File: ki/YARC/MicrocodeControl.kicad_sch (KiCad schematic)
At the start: 24 parts, among them U31 74LS32, U44 74LS574, U45 74LS574, U46 74LS157, U47 74LS157, U48 74LS193, U49 74LS193, U50 74LS139, U51 74LS32, U52 74LS32, U53 74LS157, U54 74LS32

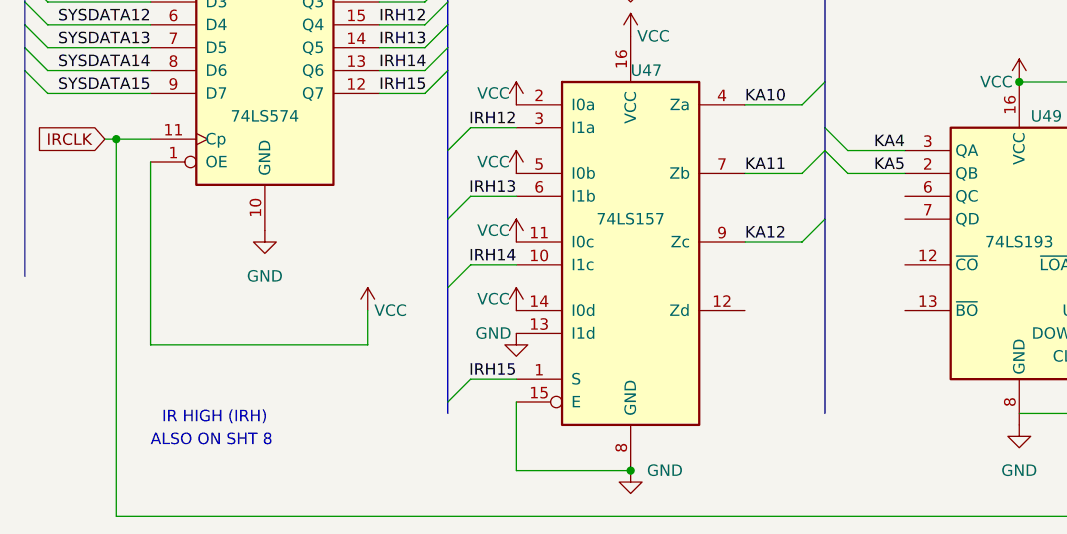
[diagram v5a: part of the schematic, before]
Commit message: Fix - add microcode RAM enables to schematic
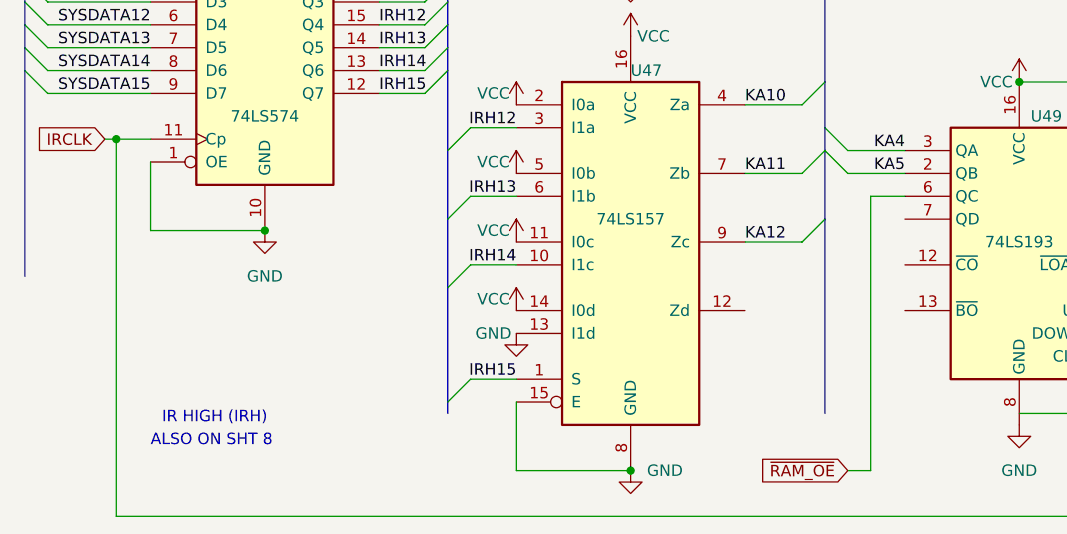
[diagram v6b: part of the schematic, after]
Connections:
- net GND: now also U44.1 (OE)
- net VCC: no longer U44.1 (OE)
- net ~{RAM_OE}: now reaches U49.6 (QC)
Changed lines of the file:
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@@
   (junction (at 209.55 67.31) (diameter 0) (color 0 0 0 0)
   )
+  (junction (at 40.64 170.18) (diameter 0) (color 0 0 0 0)
+  )
   (junction (at 209.55 29.21) (diameter 0) (color 0 0 0 0)
   )
@@
     (stroke (width 0) (type default) (color 0 0 0 0))
   )
-  (wire (pts (xy 52.07 179.07) (xy 52.07 182.88))
-    (stroke (width 0) (type default) (color 0 0 0 0))
-  )
   (bus (pts (xy 13.97 144.78) (xy 13.97 142.24))
     (stroke (width 0) (type default) (color 0 0 0 0))
@@
     (stroke (width 0) (type default) (color 0 0 0 0))
   )
-  (wire (pts (xy 27.94 182.88) (xy 52.07 182.88))
-    (stroke (width 0) (type default) (color 0 0 0 0))
-  )
   (wire (pts (xy 100.33 124.46) (xy 93.98 124.46))
     (stroke (width 0) (type default) (color 0 0 0 0))
@@
     (stroke (width 0) (type default) (color 0 0 0 0))
   )
+  (wire (pts (xy 105.41 196.85) (xy 107.95 196.85))
+    (stroke (width 0) (type default) (color 0 0 0 0))
+  )
   (wire (pts (xy 55.88 38.1) (xy 86.36 38.1))
     (stroke (width 0) (type default) (color 0 0 0 0))
@@
     (stroke (width 0) (type default) (color 0 0 0 0))
   )
+  (wire (pts (xy 27.94 170.18) (xy 40.64 170.18))
+    (stroke (width 0) (type default) (color 0 0 0 0))
+  )
   (wire (pts (xy 142.24 143.51) (xy 142.24 179.07))
     (stroke (width 0) (type default) (color 0 0 0 0))
@@
     (stroke (width 0) (type default) (color 0 0 0 0))
   )
-  (wire (pts (xy 27.94 162.56) (xy 27.94 182.88))
-    (stroke (width 0) (type default) (color 0 0 0 0))
-  )
   (wire (pts (xy 137.16 181.61) (xy 149.86 181.61))
     (stroke (width 0) (type default) (color 0 0 0 0))
@@
     (stroke (width 0) (type default) (color 0 0 0 0))
   )
+  (wire (pts (xy 107.95 166.37) (xy 107.95 196.85))
+    (stroke (width 0) (type default) (color 0 0 0 0))
+  )
   (wire (pts (xy 229.87 39.37) (xy 245.11 39.37))
     (stroke (width 0) (type default) (color 0 0 0 0))
@@
     (stroke (width 0) (type default) (color 0 0 0 0))
   )
+  (wire (pts (xy 111.76 166.37) (xy 107.95 166.37))
+    (stroke (width 0) (type default) (color 0 0 0 0))
+  )
   (wire (pts (xy 160.02 85.09) (xy 190.5 85.09))
     (stroke (width 0) (type default) (color 0 0 0 0))
@@
     (stroke (width 0) (type default) (color 0 0 0 0))
   )
+  (wire (pts (xy 27.94 162.56) (xy 27.94 170.18))
+    (stroke (width 0) (type default) (color 0 0 0 0))
+  )
   (wire (pts (xy 209.55 36.83) (xy 209.55 29.21))
     (stroke (width 0) (type default) (color 0 0 0 0))
@@
   (label "KX3" (at 30.48 38.1 180)
     (effects (font (size 1.27 1.27)) (justify right bottom))
+  )
+  (global_label "~{RAM_OE}" (shape input) (at 105.41 196.85 180) (fields_autoplaced)
+    (effects (font (size 1.27 1.27)) (justify right))
+    (property "Intersheet References" "${INTERSHEET_REFS}" (id 0) (at 95.7398 196.7706 0)
+      (effects (font (size 1.27 1.27)) (justify right) hide)
+    )
   )
   (global_label "~{KI3EN}" (shape input) (at 175.26 109.22 180) (fields_autoplaced)
@@
     (pin "7")
   )
-  (symbol (lib_id "power:VCC") (at 52.07 179.07 0)
-    (in_bom yes) (on_board yes)
-    (property "Reference" "#PWR049" (id 0) (at 52.07 182.88 0)
-      (effects (font (size 1.27 1.27)) hide)
-    )
-    (property "Value" "VCC" (id 1) (at 54.61 179.07 0))
-    (property "Footprint" "" (id 2) (at 52.07 179.07 0)
-      (effects (font (size 1.27 1.27)) hide)
-    )
-    (property "Datasheet" "" (id 3) (at 52.07 179.07 0)
-      (effects (font (size 1.27 1.27)) hide)
-    )
-    (pin "1")
-  )
   (symbol (lib_id "74xx:74LS32") (at 234.95 77.47 0)

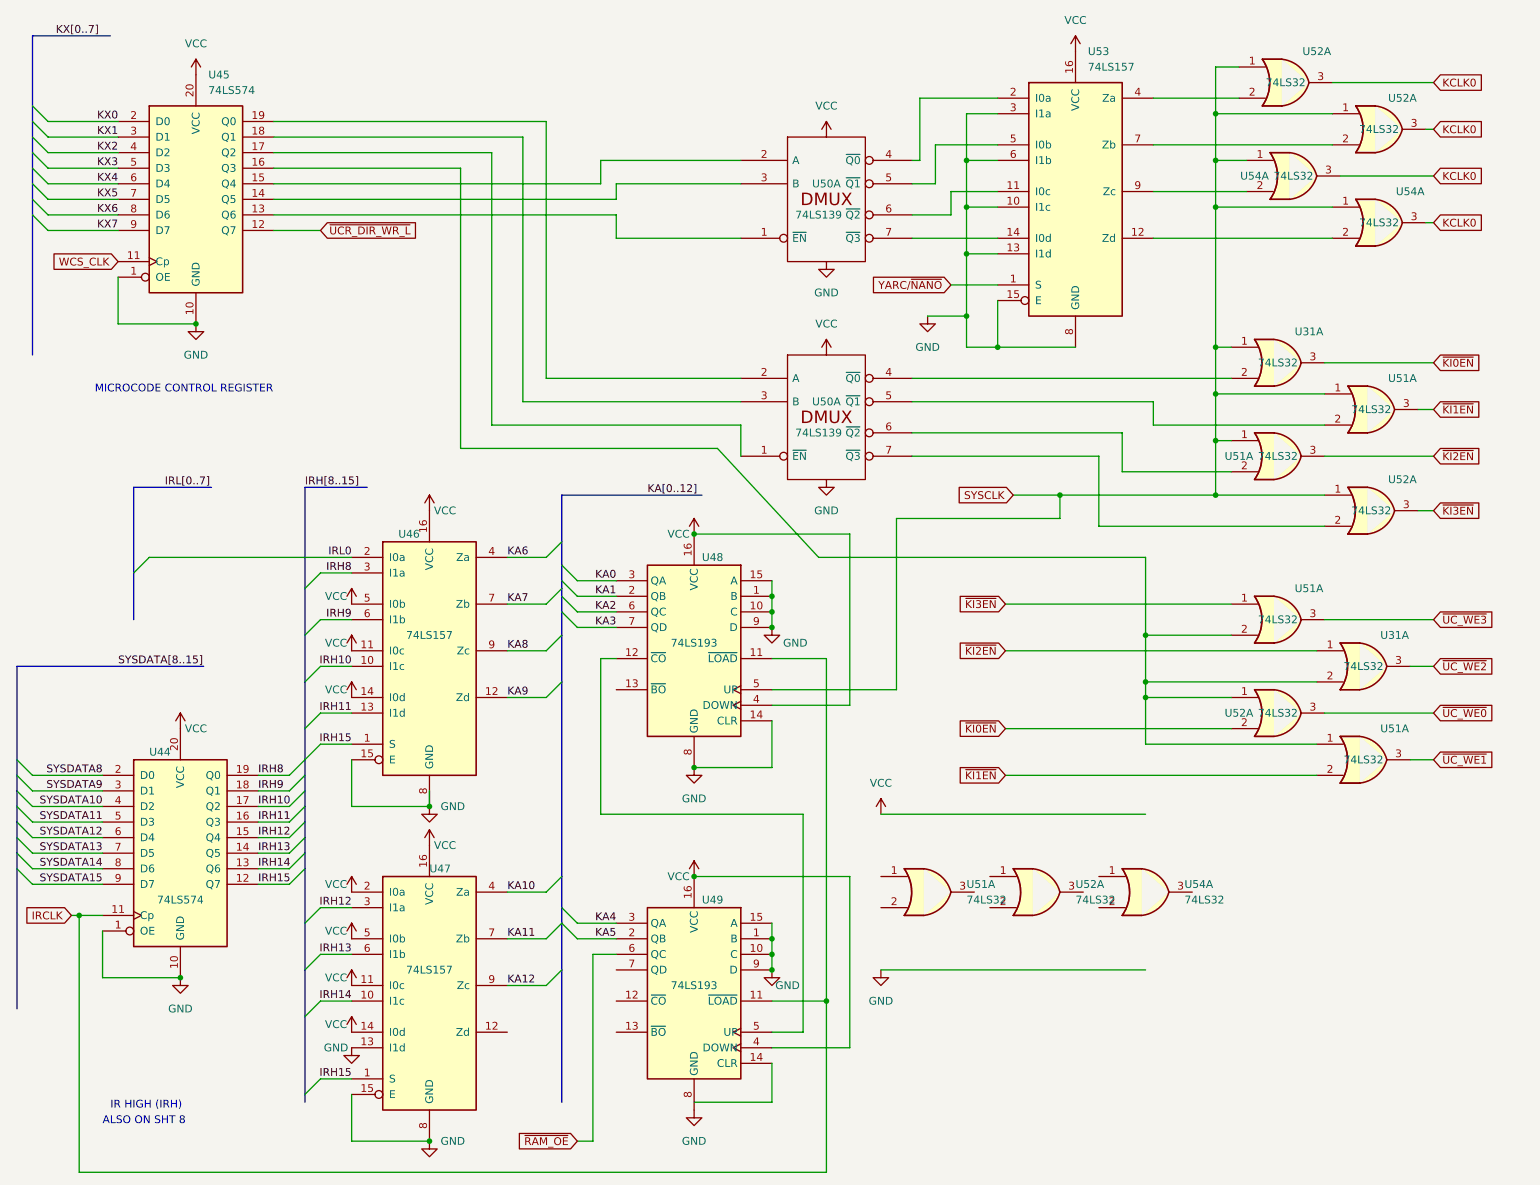
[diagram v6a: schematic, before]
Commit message: Yet more cleanup on ALU and flags design
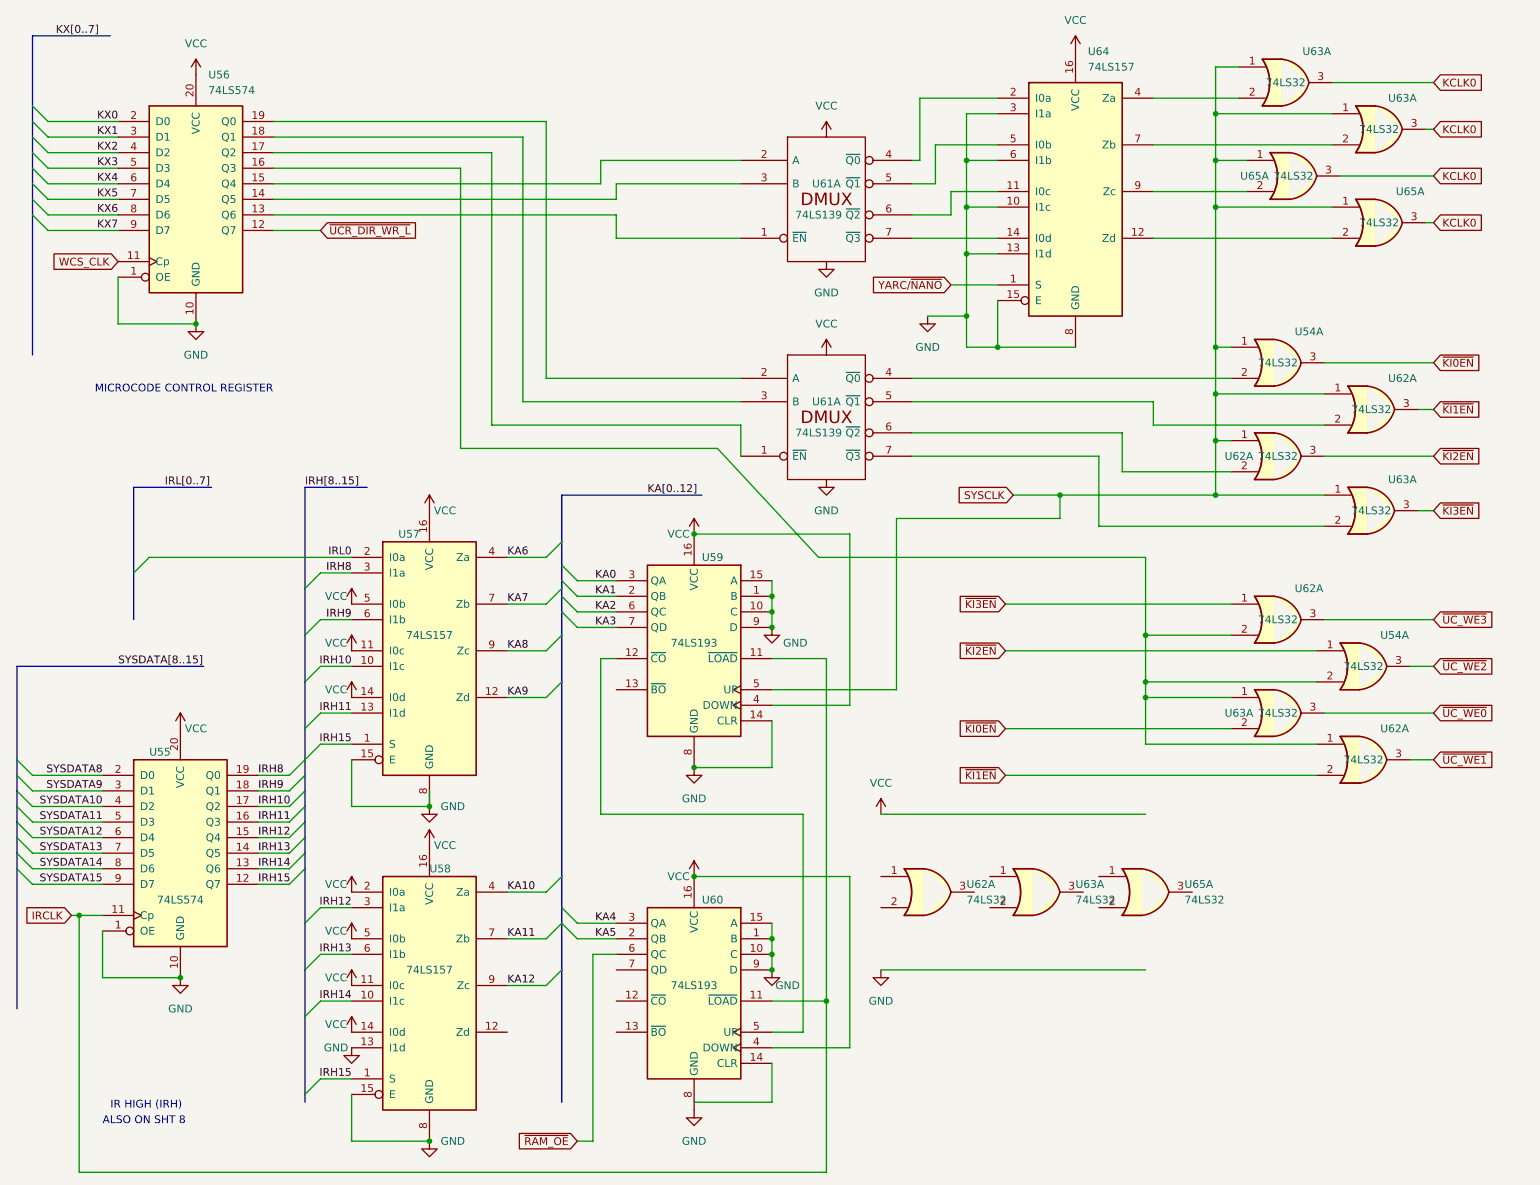
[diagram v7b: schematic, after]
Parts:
- renumbered U31 to U54, U44 to U55, U45 to U56, U46 to U57, U47 to U58, U48 to U59, U49 to U60, U50 to U61, U51 to U62, U52 to U63, U53 to U64, U54 to U65

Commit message: Large commit. Document two hardware changes to microcode controls. Adapt Nano firmware to these changes. Significantly simplify initialization logic and make it more consistent about reset.
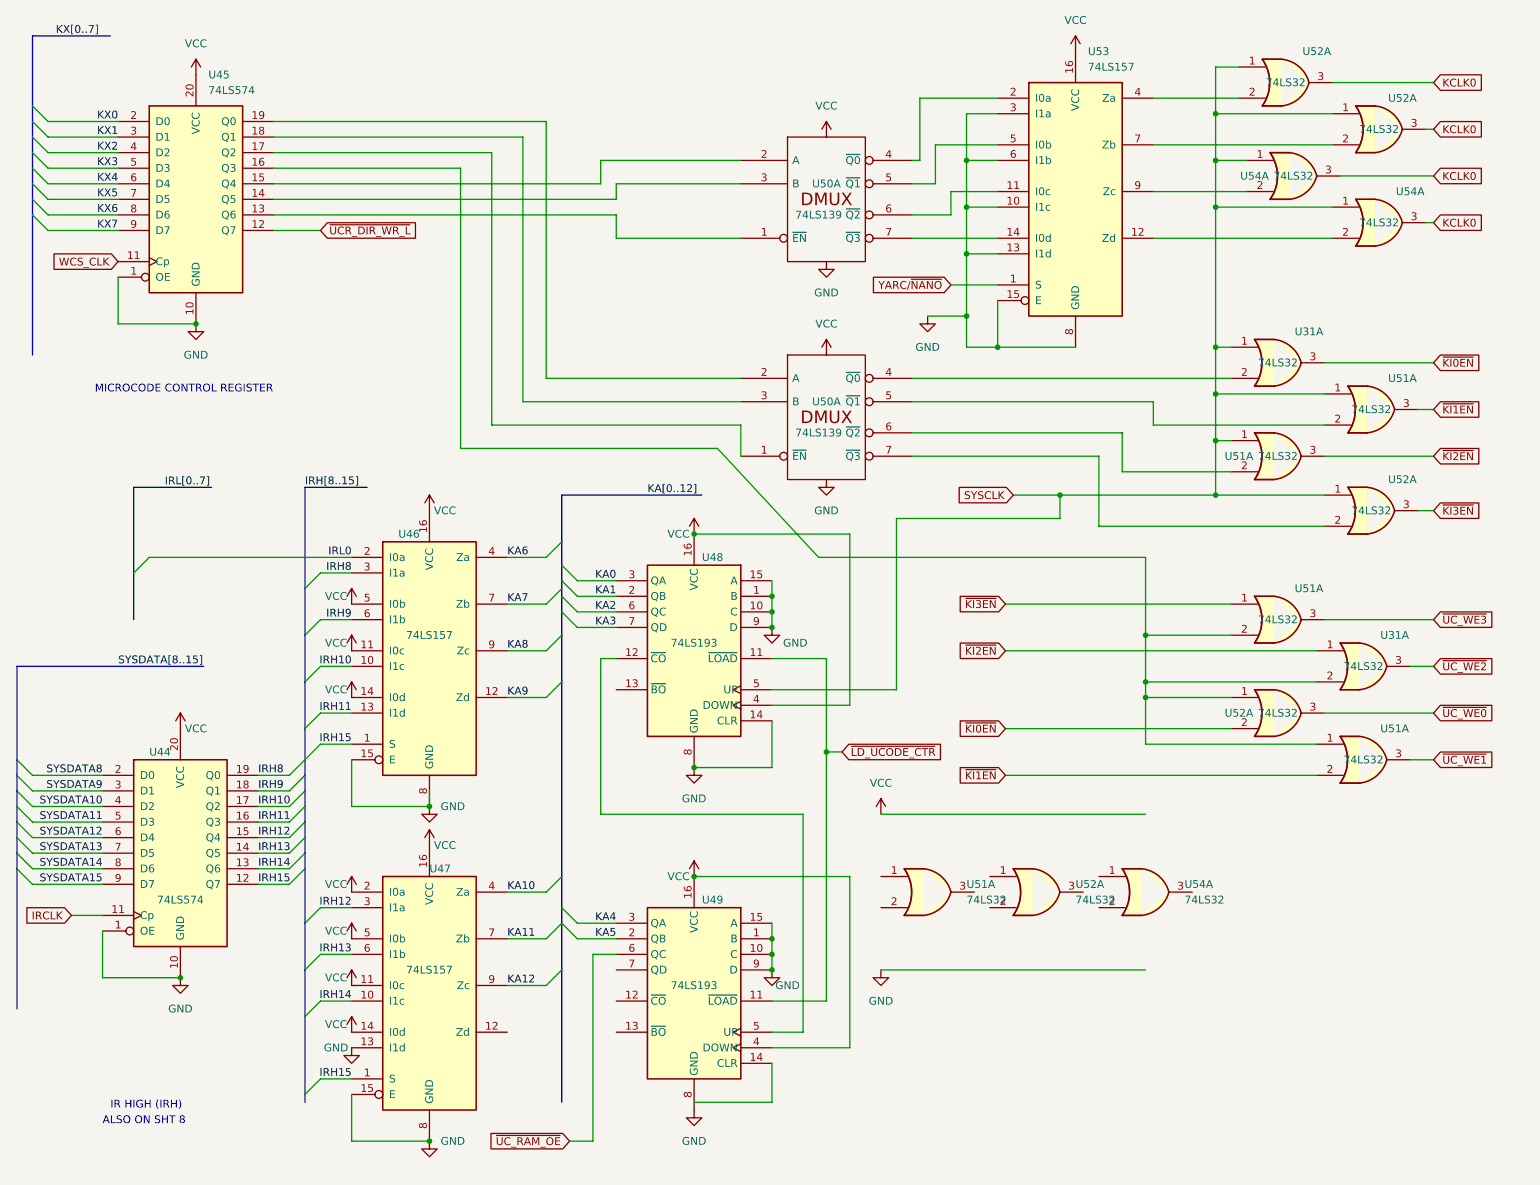
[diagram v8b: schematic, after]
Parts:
- renumbered U54 to U31, U55 to U44, U56 to U45, U57 to U46, U58 to U47, U59 to U48, U60 to U49, U61 to U50, U62 to U51, U63 to U52, U64 to U53, U65 to U54
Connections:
- net IRCLK: no longer U48.11 (~{LOAD}), U49.11 (~{LOAD})
- net ~{RAM_OE} renamed ~{UC_RAM_OE}
- new net ~{LD_UCODE_CTR}: U48.11 (~{LOAD}), U49.11 (~{LOAD})
